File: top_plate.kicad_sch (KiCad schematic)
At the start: 32 parts, among them J35 Osc Out, J36 Conn_02x12_Odd_Even, J37 Conn_02x12_Odd_Even, J38 Conn_02x12_Odd_Even, J39 Conn_02x12_Odd_Even, J40 Conn_01x08, J41 Conn_01x08, J50 Conn_02x18_Odd_Even, J51 Conn_02x18_Odd_Even, J52 Conn_02x18_Odd_Even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

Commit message: wip symmetric layout
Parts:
- added J83, J84: Output, Connector_PinHeader_2.54mm:PinHeader_2x04_P2.54mm_Vertical, symbol Connector_Generic:Conn_02x04_Odd_Even
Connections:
- new net: J84.1 (Pin_1), J84.2 (Pin_2)
- new net: J84.3 (Pin_3), J84.4 (Pin_4)
- new net: J84.5 (Pin_5), J84.6 (Pin_6)
- new net: J84.7 (Pin_7), J84.8 (Pin_8)
- new net: J83.1 (Pin_1), J83.2 (Pin_2)
- new net: J83.3 (Pin_3), J83.4 (Pin_4)
- new net: J83.5 (Pin_5), J83.6 (Pin_6)
- new net: J83.7 (Pin_7), J83.8 (Pin_8)
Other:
- note added: "18x20 Matrix"
- note added: "Passtrough"
- note removed: "18x22 Matrix"
- moved on the sheet: C18, C19, J35, J36, J37, J38, J39, J56, J57, J58, J59, RV3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

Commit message: wip assemblying everything 2
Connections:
- net GNDA: now also J58.1 (Pin_1), J58.2 (Pin_2), J59.1 (Pin_1), J59.2 (Pin_2)
- net VDDA: now also J56.1 (Pin_1), J56.2 (Pin_2), J57.1 (Pin_1), J57.2 (Pin_2)
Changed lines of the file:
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@@
+	)
+	(symbol
+		(lib_id "power:VDDA")
+		(at 62.23 24.13 0)
+		(unit 1)
+		(exclude_from_sim no)
+		(in_bom yes)
+		(on_board yes)
+		(dnp no)
+		(fields_autoplaced yes)
+		(property "Reference" "#PWR026"
+			(at 62.23 27.94 0)
+			(effects
+				(font
+					(size 1.27 1.27)
+				)
+				(hide yes)
+			)
+		)
+		(property "Value" "VDDA"
+			(at 62.23 19.05 0)
+			(effects
+				(font
+					(size 1.27 1.27)
+				)
+			)
+		)
+		(property "Footprint" ""
+			(at 62.23 24.13 0)
+			(effects
+				(font
+					(size 1.27 1.27)
+				)
+				(hide yes)
+			)
+		)
+		(property "Datasheet" ""
+			(at 62.23 24.13 0)
+			(effects
+				(font
+					(size 1.27 1.27)
+				)
+				(hide yes)
+			)
+		)
+		(property "Description" "Power symbol creates a global label with name \"VDDA\""
+			(at 62.23 24.13 0)
+			(effects
+				(font
+					(size 1.27 1.27)
+				)
+				(hide yes)
+			)
+		)
+		(pin "1"
+		)
+		(instances
+			(project "kleingorium"
+				(path "/01c1f2c1-4d06-4880-847a-9ab55552e3fd/44f3fb3f-0223-4473-937a-c9802bdd1286"
+					(reference "#PWR026")
+					(unit 1)
+				)
+			)
+		)
 	)
 	(symbol
@@
 					(unit 1)
 				)
+			)
+		)
+	)
+	(symbol
+		(lib_id "power:GNDA")
+		(at 77.47 40.64 0)
+		(unit 1)
+		(exclude_from_sim no)
+		(in_bom yes)
+		(on_board yes)
+		(dnp no)
+		(fields_autoplaced yes)
+		(property "Reference" "#PWR025"
+			(at 77.47 46.99 0)
+			(effects
+				(font
+					(size 1.27 1.27)
+				)
+				(hide yes)
+			)
+		)
+		(property "Value" "GNDA"
+			(at 77.47 45.72 0)
+			(effects
+				(font
+					(size 1.27 1.27)
+				)
+			)
+		)
+		(property "Footprint" ""
+			(at 77.47 40.64 0)
+			(effects
+				(font
+					(size 1.27 1.27)
+				)
+				(hide yes)
+			)
+		)
+		(property "Datasheet" ""
+			(at 77.47 40.64 0)
+			(effects
+				(font
+					(size 1.27 1.27)
+				)
+				(hide yes)
+			)
+		)
+		(property "Description" "Power symbol creates a global label with name \"GNDA\" , analog ground"
+			(at 77.47 40.64 0)
+			(effects
+				(font
+					(size 1.27 1.27)
+				)
+				(hide yes)
+			)
+		)
+		(pin "1"
+		)
+		(instances
+			(project "kleingorium"
+				(path "/01c1f2c1-4d06-4880-847a-9ab55552e3fd/44f3fb3f-0223-4473-937a-c9802bdd1286"
+					(reference "#PWR025")
+					(unit 1)
+				)

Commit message: 3 board alignment
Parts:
- removed J72: Conn_02x18_Odd_Even, Connector_PinSocket_2.54mm:PinSocket_2x18_P2.54mm_Vertical, symbol Connector_Generic:Conn_02x18_Odd_Even
- added J87: AudioJack3, Connector_Audio:Jack_3.5mm_CUI_SJ1-3523N_Horizontal, symbol Connector_Audio:AudioJack3
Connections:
- net GNDA: now also J87.S
- net at RV5.3, U10.12: now also J87.T
- net at RV6.3, U10.10: now also J87.R
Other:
- note added: "16x20 Matrix"
- note removed: "18x20 Matrix"
- moved on the sheet: J40, J41, RN1, RN2, RV5, RV6, U10E, U10F

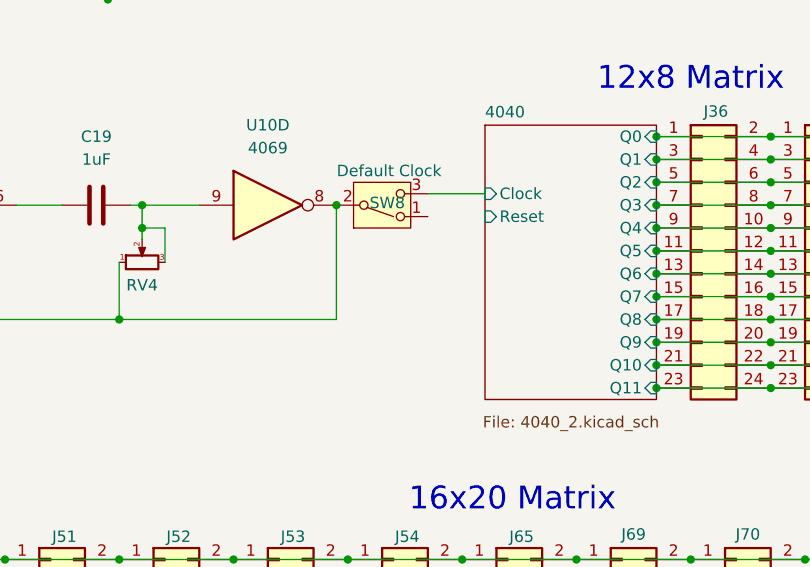
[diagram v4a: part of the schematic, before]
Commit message: add 4040 Clk Rst connector
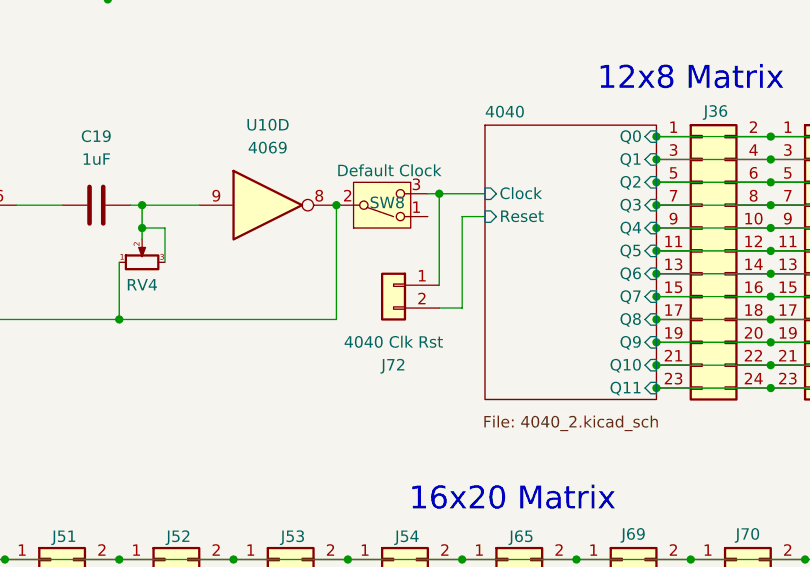
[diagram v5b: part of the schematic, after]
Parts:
- added J72: 4040 Clk Rst, Connector_PinHeader_2.54mm:PinHeader_1x02_P2.54mm_Vertical, symbol Connector_Generic:Conn_01x02
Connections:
- net 4040/Clock: now also J72.1 (Pin_1)
- net 4040/Reset: now also J72.2 (Pin_2)
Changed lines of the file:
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@@
 	)
 	(junction
+		(at 90.17 100.33)
+		(diameter 0)
+		(color 0 0 0 0)
+	)
+	(junction
 		(at 54.61 146.05)
 		(diameter 0)
@@
 	(wire
 		(pts
+			(xy 90.17 100.33) (xy 90.17 110.49)
+		)
+		(stroke
+			(width 0)
+			(type default)
+		)
+	)
+	(wire
+		(pts
 			(xy 152.4 96.52) (xy 165.1 96.52)
 		)
@@
 	(wire
 		(pts
-			(xy 88.9 100.33) (xy 95.25 100.33)
+			(xy 88.9 100.33) (xy 90.17 100.33)
 		)
 		(stroke
@@
 	(wire
 		(pts
+			(xy 90.17 113.03) (xy 92.71 113.03)
+		)
+		(stroke
+			(width 0)
+			(type default)
+		)
+	)
+	(wire
+		(pts
 			(xy 213.36 97.79) (xy 217.17 97.79)
 		)
@@
 	(wire
 		(pts
+			(xy 90.17 100.33) (xy 95.25 100.33)
+		)
+		(stroke
+			(width 0)
+			(type default)
+		)
+	)
+	(wire
+		(pts
 			(xy 80.01 153.67) (xy 92.71 153.67)
 		)
@@
 		)
 	)
+	(wire
+		(pts
+			(xy 92.71 102.87) (xy 95.25 102.87)
+		)
+		(stroke
+			(width 0)
+			(type default)
+		)
+	)
+	(wire
+		(pts
+			(xy 92.71 113.03) (xy 92.71 102.87)
+		)
+		(stroke
+			(width 0)
+			(type default)
+		)
+	)
 	(symbol
 		(lib_id "power:GNDA")
@@
 				)
 			)
+		)
+	)
+	(symbol
+		(lib_id "Connector_Generic:Conn_01x02")
+		(at 85.09 110.49 0)
+		(mirror y)
+		(unit 1)
+		(exclude_from_sim no)
+		(in_bom yes)
+		(on_board yes)
+		(dnp no)
+		(property "Reference" "J72"
+			(at 85.09 119.38 0)
+			(effects
+				(font
+					(size 1.27 1.27)
+				)
+			)
+		)
+		(property "Value" "4040 Clk Rst"
+			(at 85.09 116.84 0)
+			(effects
+				(font
+					(size 1.27 1.27)
+				)
+			)
+		)
+		(property "Footprint" "Connector_PinHeader_2.54mm:PinHeader_1x02_P2.54mm_Vertical"
+			(at 85.09 110.49 0)
+			(effects
+				(font
+					(size 1.27 1.27)
+				)
+				(hide yes)
+			)
+		)
+		(property "Datasheet" "~"
+			(at 85.09 110.49 0)
+			(effects
+				(font
+					(size 1.27 1.27)
+				)
+				(hide yes)
+			)
+		)
+		(property "Description" "Generic connector, single row, 01x02, script generated (kicad-library-utils/schlib/autogen/connector/)"
+			(at 85.09 110.49 0)
+			(effects
+				(font
+					(size 1.27 1.27)
+				)
+				(hide yes)
+			)
+		)
+		(pin "2"
+		)
+		(pin "1"
+		)
+		(instances
+			(project ""
+				(path "/01c1f2c1-4d06-4880-847a-9ab55552e3fd/44f3fb3f-0223-4473-937a-c9802bdd1286"
+					(reference "J72")
+					(unit 1)
+				)
+			)

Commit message: fix alignment issues
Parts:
- added J82: Conn_02x18_Odd_Even, Connector_PinHeader_2.54mm:PinHeader_2x18_P2.54mm_Vertical, symbol Connector_Generic:Conn_02x18_Odd_Even
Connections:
- net at J50.1 (Pin_1), J50.2 (Pin_2), J51.1 (Pin_1)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: now also J82.1 (Pin_1), J82.2 (Pin_2)
- net at J50.10 (Pin_10), J50.9 (Pin_9), J51.10 (Pin_10)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: now also J82.10 (Pin_10), J82.9 (Pin_9)
- net at J50.11 (Pin_11), J50.12 (Pin_12), J51.11 (Pin_11)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: now also J82.11 (Pin_11), J82.12 (Pin_12)
- net at J50.13 (Pin_13), J50.14 (Pin_14), J51.13 (Pin_13)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: now also J82.13 (Pin_13), J82.14 (Pin_14)
- net at J50.15 (Pin_15), J50.16 (Pin_16), J51.15 (Pin_15)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: now also J82.15 (Pin_15), J82.16 (Pin_16)
- net at J50.17 (Pin_17), J50.18 (Pin_18), J51.17 (Pin_17)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: now also J82.17 (Pin_17), J82.18 (Pin_18)
- net at J50.19 (Pin_19), J50.20 (Pin_20), J51.19 (Pin_19)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: now also J82.19 (Pin_19), J82.20 (Pin_20)
- net at J50.21 (Pin_21), J50.22 (Pin_22), J51.21 (Pin_21)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: now also J82.21 (Pin_21), J82.22 (Pin_22)
- net at J50.23 (Pin_23), J50.24 (Pin_24), J51.23 (Pin_23)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: now also J82.23 (Pin_23), J82.24 (Pin_24)
- net at J50.25 (Pin_25), J50.26 (Pin_26), J51.25 (Pin_25)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: now also J82.25 (Pin_25), J82.26 (Pin_26)
- net at J50.27 (Pin_27), J50.28 (Pin_28), J51.27 (Pin_27)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: now also J82.27 (Pin_27), J82.28 (Pin_28)
- net at J50.29 (Pin_29), J50.30 (Pin_30), J51.29 (Pin_29)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: now also J82.29 (Pin_29), J82.30 (Pin_30)
- net at J50.3 (Pin_3), J50.4 (Pin_4), J51.3 (Pin_3)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: now also J82.3 (Pin_3), J82.4 (Pin_4)
- net at J50.31 (Pin_31), J50.32 (Pin_32), J51.31 (Pin_31)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: now also J82.31 (Pin_31), J82.32 (Pin_32)
- net at J50.33 (Pin_33), J50.34 (Pin_34), J51.33 (Pin_33)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: now also J82.33 (Pin_33), J82.34 (Pin_34)
- net at J50.35 (Pin_35), J50.36 (Pin_36), J51.35 (Pin_35)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: now also J82.35 (Pin_35), J82.36 (Pin_36)
- net at J50.5 (Pin_5), J50.6 (Pin_6), J51.5 (Pin_5)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: now also J82.5 (Pin_5), J82.6 (Pin_6)
- net at J50.7 (Pin_7), J50.8 (Pin_8), J51.7 (Pin_7)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: now also J82.7 (Pin_7), J82.8 (Pin_8)

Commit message: 18x20 design
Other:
- note added: "18x20 Matrix"
- note removed: "16x20 Matrix"
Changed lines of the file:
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@@
 		)
 	)
-	(text "16x20 Matrix"
+	(text "18x20 Matrix"
 		(exclude_from_sim no)
 		(at 98.298 134.366 0)
